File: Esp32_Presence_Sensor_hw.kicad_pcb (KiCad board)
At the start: 2 copper layers, 63.7 x 61.7 mm, 101 parts, among them J1 USB_C_16P, J2 Screw_Terminal_01x04, J3 0R, J4 0R, J5 0R, J6 0R, J7 0R, J8 0R, J9 Conn_01x03_Male, K1 G5LE-1, Q1 2SC1815/HF, Q2 2SC1815/HF, SW1 SW_3.5x6x2.5, SW2 SW_3.5x6x2.5, U1 ESP32-C3, U2 SYN470R, U3 LD2410, U4 CR1510, U5 DS18B20, U6 EE13-5V, U7 RT9193, U8 PC817, U9 2.2inch_TFT_ILI9341_SPI, Y1 40MHz

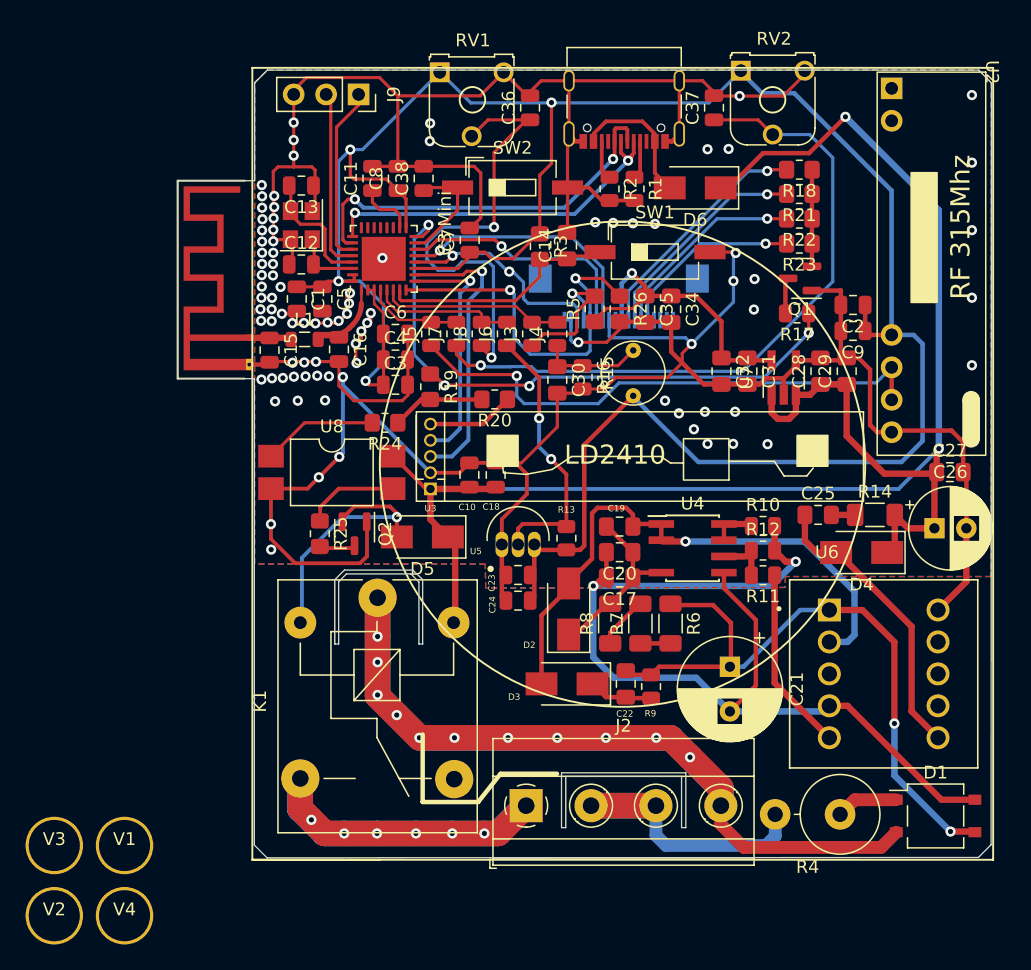
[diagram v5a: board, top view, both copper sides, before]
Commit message: modified block LCD (sch & pcb)
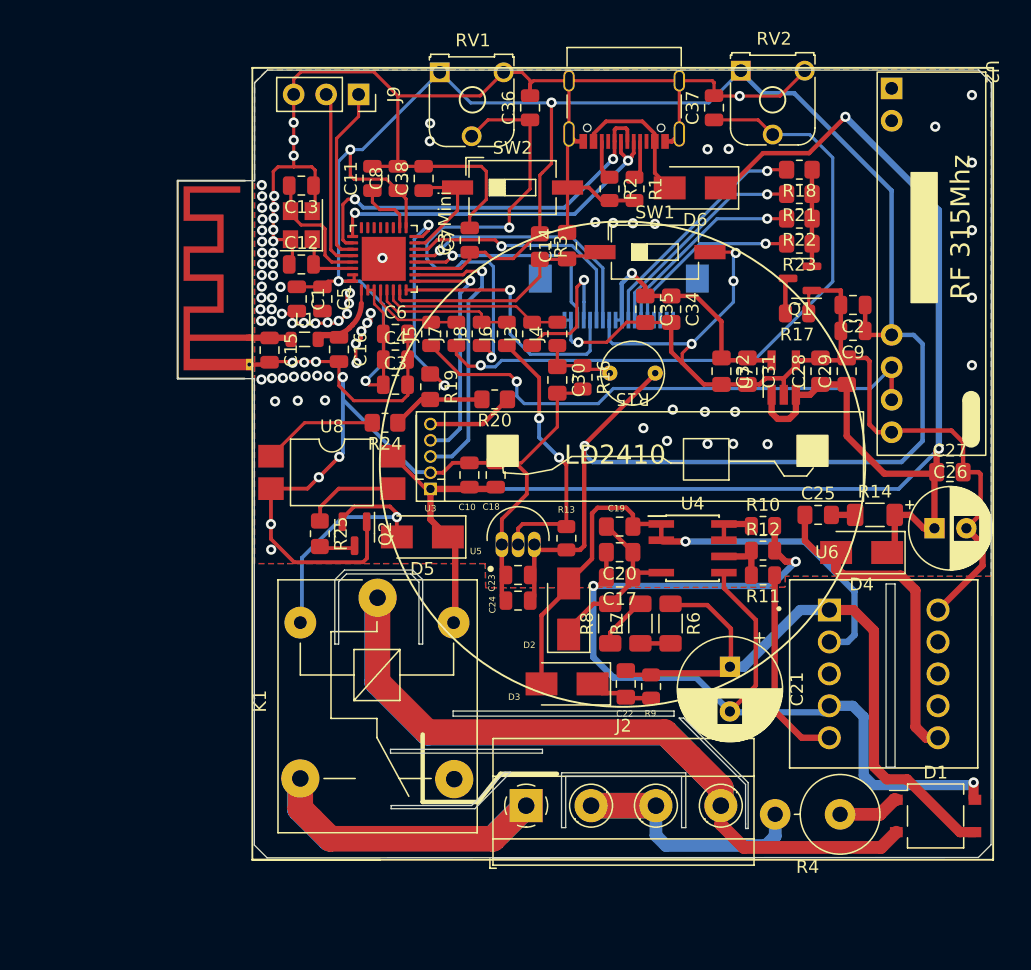
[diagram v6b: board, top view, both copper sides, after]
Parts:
- removed R26, R5: 0R, Resistor_SMD:R_0805_2012Metric_Pad1.20x1.40mm_HandSolder
- removed V1, V2, V3, V4: Vit, Lib_Mr_DH:Vit
- moved R15 0.05 mm to (138.3, 91.8), turned to 180 degrees
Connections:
- R17 pad 1: /LCD_BL -> GND
- R19 pad 1: /LCD_BL -> /RELAY
- U1 pad 16: /LCD_BL -> /RELAY
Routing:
- net /LCD_BL: track 49.1 -> 0.00 mm, vias 4 -> 0
- net /RELAY: track 0.00 -> 17.3 mm, vias 0 -> 2
- net /LCD_CS0: track 28.8 -> 21.0 mm, vias 2 -> 1
- net +3V3: track 192.5 -> 197.7 mm, vias 4 -> 5
- net +3.3V: track 25.2 -> 20.4 mm
- net /Out_Lamp: track 45.4 -> 49.2 mm, vias 6 -> 0
- net Earth: track 77.0 -> 80.7 mm, vias 2 -> 3
- net Net-(D4-A): track 22.7 -> 26.0 mm
- net /R_Photo: track 8.13 -> 6.10 mm
- net Net-(R11-Pad1): track 14.5 -> 15.8 mm
- net /L: track 94.3 -> 93.1 mm, vias 11 -> 0
- net /LCD_SCL: track 16.5 -> 17.5 mm, vias 2 -> 1
- net /LCD_DC: track 11.7 -> 11.0 mm
- net /ADC_RV1: track 36.3 -> 36.9 mm
- net GND: track 306.4 -> 306.2 mm, vias 91 -> 90
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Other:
- outline, holes or cut-outs redrawn
